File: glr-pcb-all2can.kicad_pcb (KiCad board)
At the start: 2 copper layers, 61 x 33.5 mm, 76 parts, among them IC1 ATA6561-GAQW-N, IC2 ZMR330FTA, IC4 STM32C092KCT6, IC5 AP64060WU-7, IC6 AP64060WU-7, J1 Conn_02x02_Counter_Clockwise_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, J2 Conn_02x02_Counter_Clockwise_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, J3 Conn_02x02_Counter_Clockwise_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, J4 Conn_02x02_Counter_Clockwise_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, J5 Conn_01x04, J6 Conn_01x02, J7 Conn_01x02, J8 62701021621

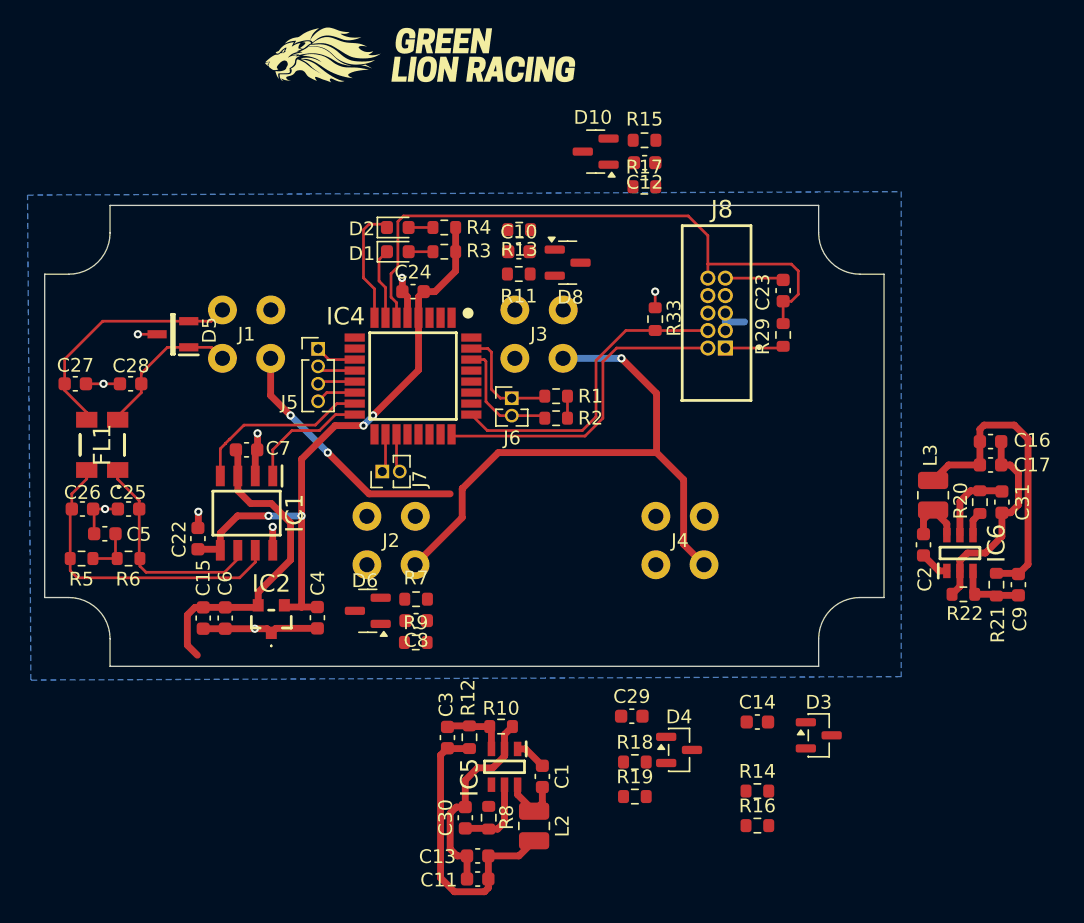
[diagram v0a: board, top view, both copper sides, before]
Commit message: routing mostly done
* missed that there need to be holes in bopla housing
* add stm32 chip datasheet
* remove unused würth library
* change pins on chip of sensor data input
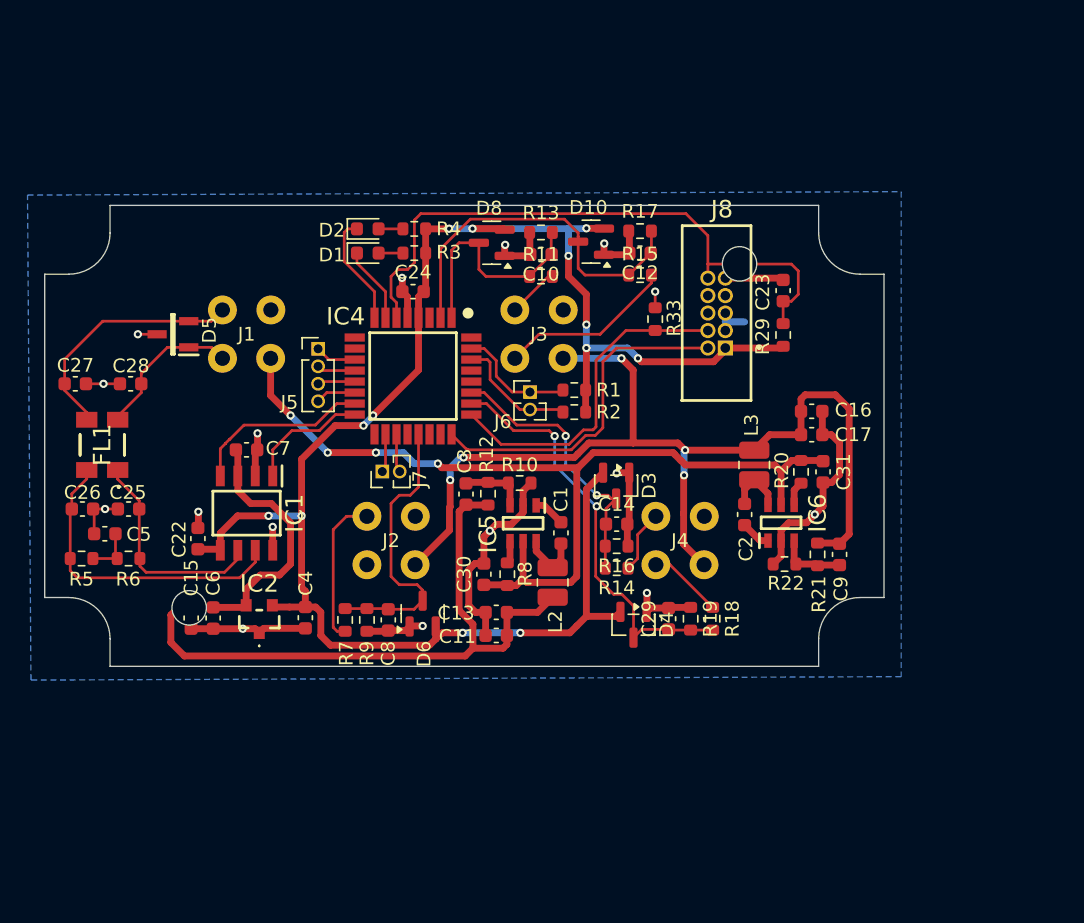
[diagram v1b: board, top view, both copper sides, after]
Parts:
- added REF**: MountingHole_2.5mm, MountingHole:MountingHole_2.5mm, F.Cu at (120.3, 113.4)
- added REF**: MountingHole_2.5mm, MountingHole:MountingHole_2.5mm, F.Cu at (160.3, 88.4)
- G***: moved to B.Cu
- moved G*** 42.1 mm to (127.1, 114.1), turned to 180 degrees
- moved D3 23.4 mm to (151.4, 104.5), turned to -90 degrees
- moved R16 22.7 mm to (151.4, 108.9), turned to 180 degrees
- moved R14 19.2 mm to (151.4, 110.5), turned to 180 degrees
- moved L2 17.8 mm to (146.8, 111.5)
- moved C1 17.8 mm to (147.3, 107.9)
- moved C11 17.8 mm to (142.7, 115.4)
- moved C3 17.8 mm to (140.4, 105.1)
- moved IC5 17.8 mm to (144.6, 107.2)
- moved R10 17.8 mm to (144.3, 104.3)
- moved R12 17.8 mm to (142.1, 105.1)
- moved C13 17.8 mm to (142.7, 113.7)
- moved C30 17.8 mm to (141.8, 110.9)
- moved R8 17.8 mm to (143.4, 110.9)
- moved C14 17.6 mm to (151.4, 107.3)
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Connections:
- IC4 pad 1: unconnected-(IC4-PB9-Pad1) -> IC_IN_2
- IC4 pad 2: unconnected-(IC4-PC14-OSCX_IN-Pad2) -> IC_IN_3
- IC4 pad 21: IC_IN_3 -> IC_IN_1
- IC4 pad 22: IC_IN_2 -> unconnected-(IC4-PA11_[PA9]-Pad22)
- IC4 pad 23: IC_IN_1 -> unconnected-(IC4-PA12_[PA10]-Pad23)
- IC4 pad 26: unconnected-(IC4-PA15-Pad26) -> IC_IN_5
- IC4 pad 27: unconnected-(IC4-PB3-Pad27) -> IC_IN_4
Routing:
- net +3V3: track 51.6 -> 126.8 mm, vias 4 -> 13
- net +24V: track 30.4 -> 66.8 mm, vias 2 -> 4
- net IC_IN_5: track 0.00 -> 30.5 mm, vias 0 -> 2
- net IC_IN_3: track 0.00 -> 26.6 mm
- net GND: track 63.0 -> 86.9 mm, vias 9 -> 16
- net +5V: track 44.7 -> 67.6 mm
- net IC_IN_1: track 0.00 -> 21.0 mm
- net IC_IN_4: track 0.00 -> 20.6 mm, vias 0 -> 2
- net IC_IN_2: track 0.00 -> 16.7 mm
- net /Input filter/3_IN: track 0.00 -> 12.8 mm
- net /Input filter/1_IN: track 0.00 -> 10.9 mm
- net +XXV: track 66.2 -> 73.6 mm, vias 1 -> 5
- net /Input filter/5_IN: track 0.00 -> 5.41 mm
- net /Input filter/4_IN: track 0.00 -> 4.61 mm
- net /Input filter/2_IN: track 0.00 -> 3.71 mm
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
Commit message: move parts out of holes
* check drc
* fix silk texts
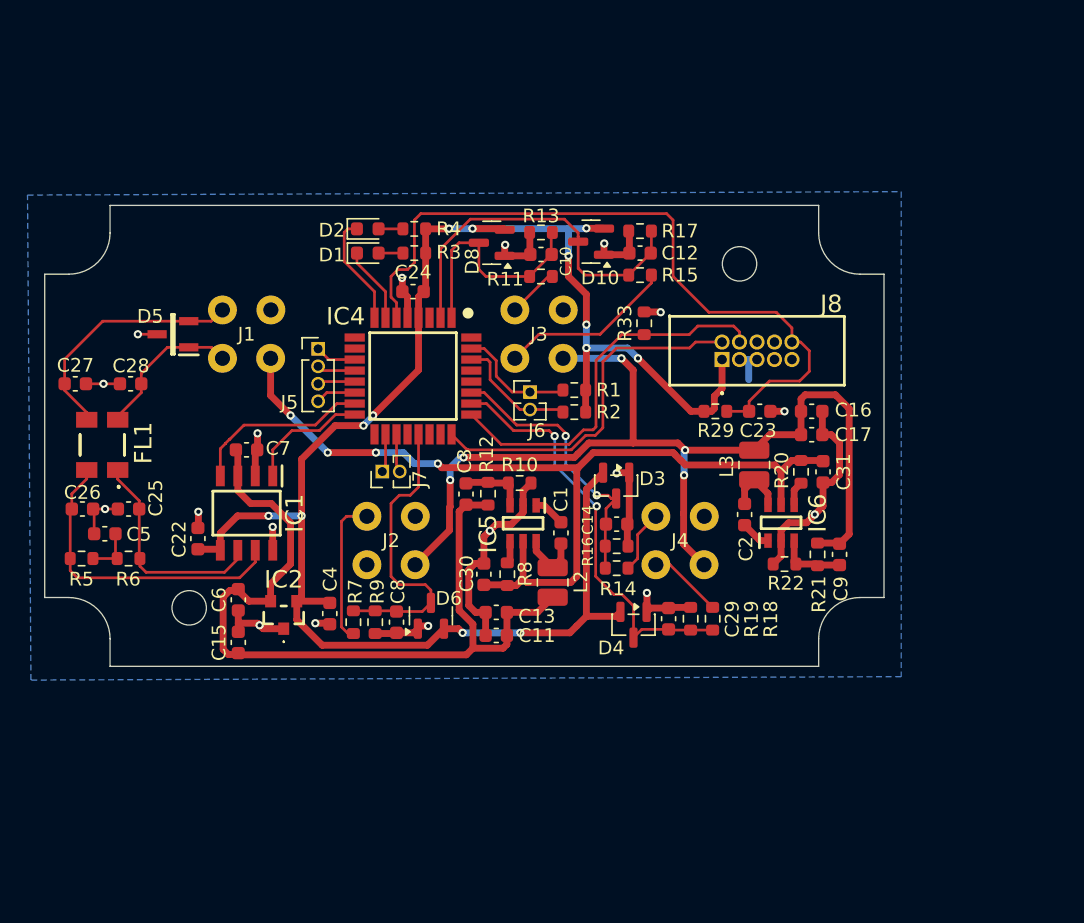
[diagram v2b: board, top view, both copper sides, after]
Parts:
- moved G*** 26.5 mm to (127.0, 87.6)
- moved C23 8.94 mm to (161.8, 99.1), turned to 180 degrees
- moved R29 7.42 mm to (158.6, 99.1), turned to 0 degrees
- moved C15 3.86 mm to (123.9, 115.9), turned to 90 degrees
- moved C6 2.26 mm to (123.9, 112.8)
- moved C4 1.80 mm to (130.6, 113.8)
- moved IC2 1.80 mm to (127.2, 113.9)
- moved J8 0.87 mm to (159.1, 95.3), turned to 0 degrees
- moved R33 0.85 mm to (153.4, 92.7)
- moved D6 0.62 mm to (137.9, 114.0)
- moved C8 0.62 mm to (135.4, 114.4)
- moved R7 0.62 mm to (132.3, 114.4)
- moved R9 0.62 mm to (133.8, 114.4)
- renumbered REF** to H1, REF** to H2
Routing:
- net NRST: track 45.1 -> 53.5 mm
- net GND: track 86.9 -> 81.1 mm, vias 16 -> 18
- net +5V: track 67.6 -> 61.9 mm
- net SWCLK: track 24.3 -> 27.7 mm
- net SWDIO: track 25.0 -> 26.2 mm
- net IC_IN_1: track 21.0 -> 21.8 mm
- net +3V3: track 126.8 -> 126.2 mm

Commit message: setup as aisler project
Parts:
- moved G*** 2.09 mm to (129.0, 87.0)
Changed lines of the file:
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@@
 		(company "Green Lion Racing")
 		(comment 1 "Alexander Wallrodt")
+		(comment 4 "AISLER Project ID: XLTMZTDL")
 	)
 	(layers
@@
 	(footprint "GLR_KiCad_Library:glr-logo"
 		(layer "B.Cu")
-		(at 127 87.6 180)
+		(at 129 87 180)
 		(property "Reference" "G***"
 			(at 0 0 0)
@@
 	)
 	(gr_line
+		(start 122.75 110)
+		(end 122.75 117.5)
+		(stroke
+			(width 0.08382)
+			(type solid)
+		)
+		(layer "B.SilkS")
+	)
+	(gr_line
+		(start 152.75 110)
+		(end 122.75 110)
+		(stroke
+			(width 0.08382)
+			(type solid)
+		)
+		(layer "B.SilkS")
+	)
+	(gr_line
+		(start 152.75 110)
+		(end 152.75 117.5)
+		(stroke
+			(width 0.08382)
+			(type solid)
+		)
+		(layer "B.SilkS")
+	)
+	(gr_line
+		(start 152.75 117.5)
+		(end 122.75 117.5)
+		(stroke
+			(width 0.08382)
+			(type solid)
+		)
+		(layer "B.SilkS")
+	)
+	(gr_line
 		(start 107.9565 100.8835)
 		(end 172.7065 100.8835)
@@
 	)
 	(gr_text "${COMPANY}\n${TITLE}\n${PROJECTNAME} ${REVISION}\n${ISSUE_DATE}\n${COMMENT1}\n${COMMENT2}\n${COMMENT3}"
-		(at 169.9 96 0)
+		(at 169.25 97.25 0)
 		(layer "B.SilkS")
 		(effects
